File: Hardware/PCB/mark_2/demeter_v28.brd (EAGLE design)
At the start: 90 x 56 mm, 69 parts, among them IC1 4050, IC2 LM1117-5.0, IC3 LM1117-3.3, IC5 MCP3424, IC6 MCP23017SO, IC8 ATMEGA32U4-AU, Q1 IRLML6402, Q3 IRLML6402, Q5 IRLML6402

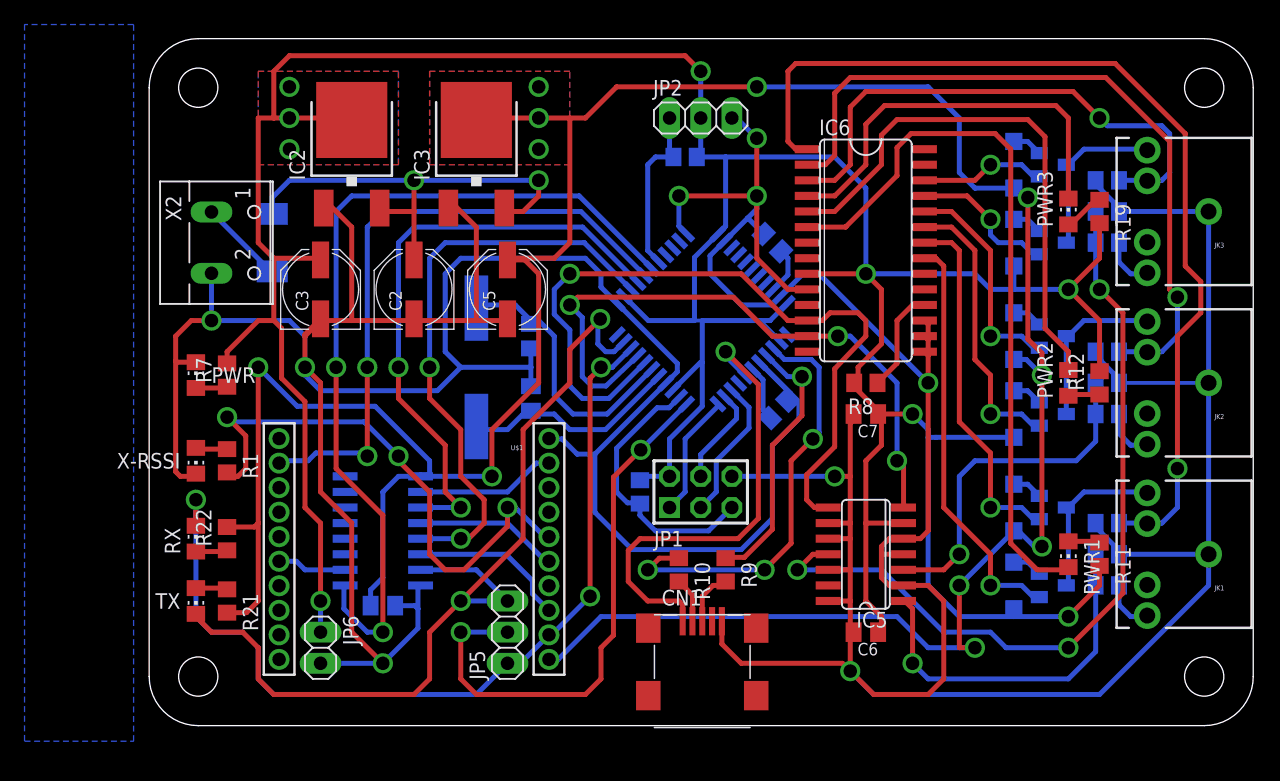
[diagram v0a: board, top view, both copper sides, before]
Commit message: 
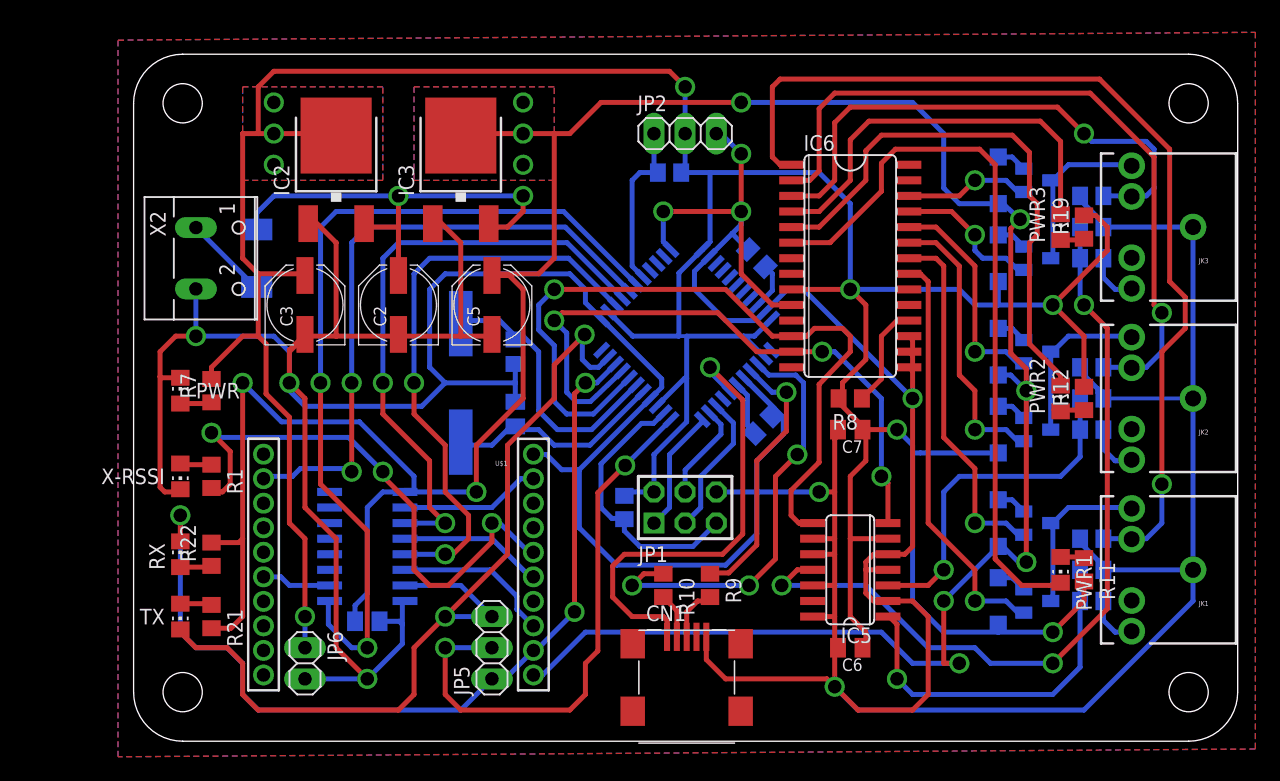
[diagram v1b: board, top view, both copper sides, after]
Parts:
- moved Q3 1.80 mm to (73.7, 25.4)
- moved Q4 1.80 mm to (73.7, 31.8)
- moved Q5 1.80 mm to (73.7, 39.4)
- moved Q6 1.80 mm to (73.7, 45.7)
- moved Q1 1.80 mm to (73.7, 11.4)
- moved Q2 1.80 mm to (73.7, 17.8)
- moved C8 1.80 mm to (50.8, 39.4)
- moved D1 1.80 mm to (10.0, 39.4)
- moved R10 1.80 mm to (43.2, 12.7)
- moved X2 1.80 mm to (6.35, 39.4)
- moved C1 1.80 mm to (51.3, 25.8)
- moved C9 1.80 mm to (31.1, 31.8)
- moved JP1 1.80 mm to (45.0, 19.1)
- moved U$1 1.80 mm to (21.6, 25.4)
- moved R22 1.80 mm to (6.35, 15.2)
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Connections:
- net GND: now also CN1.GND1, CN1.GND2, CN1.GND3, CN1.GND4
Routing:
- net +5V: track 298.7 -> 302.7 mm
- net N$23: track 3.56 -> 2.36 mm
- net N$33: track 44.3 -> 45.1 mm
- net +3V3: track 239.2 -> 239.9 mm
- net N$5: track 2.58 -> 1.95 mm
- net N$9: track 59.5 -> 60.0 mm
- added copper zone on layer 1, net GND
